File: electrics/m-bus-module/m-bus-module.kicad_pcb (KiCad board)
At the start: 2 copper layers, 86 x 31 mm, 58 parts, among them J1 North, J2 South, J3 West, J4 East, Q1 BC856B-13-F, Q2 BC846B-7-F, Q3 FDN5618P, U1 BA033CC0FP-E2, U2 MAX3486, U3 VOM452T, U4 VOM452T, U5 MC33072ADR2G, U6 LM4040DIM3-5.0/NOPB

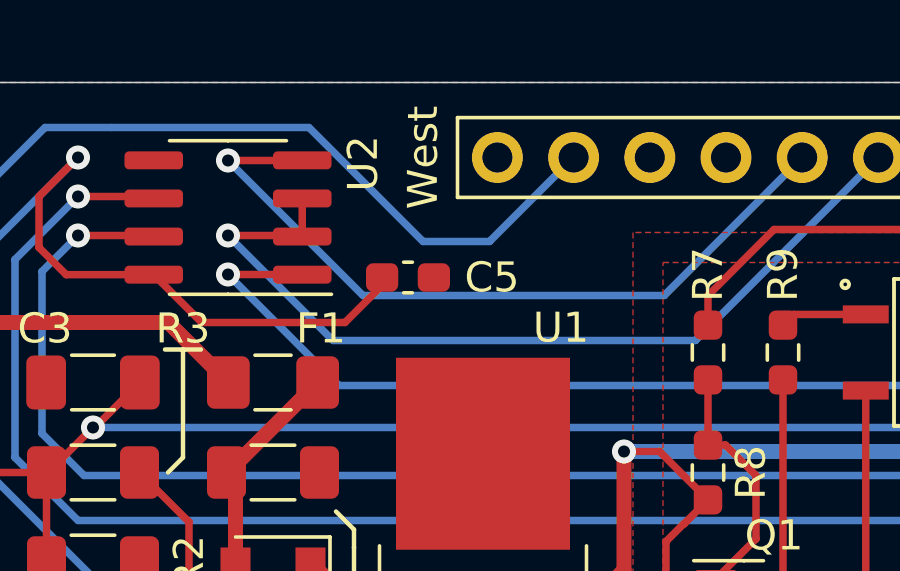
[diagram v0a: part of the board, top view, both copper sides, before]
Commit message: Fix all ERC and DRC warnings during build
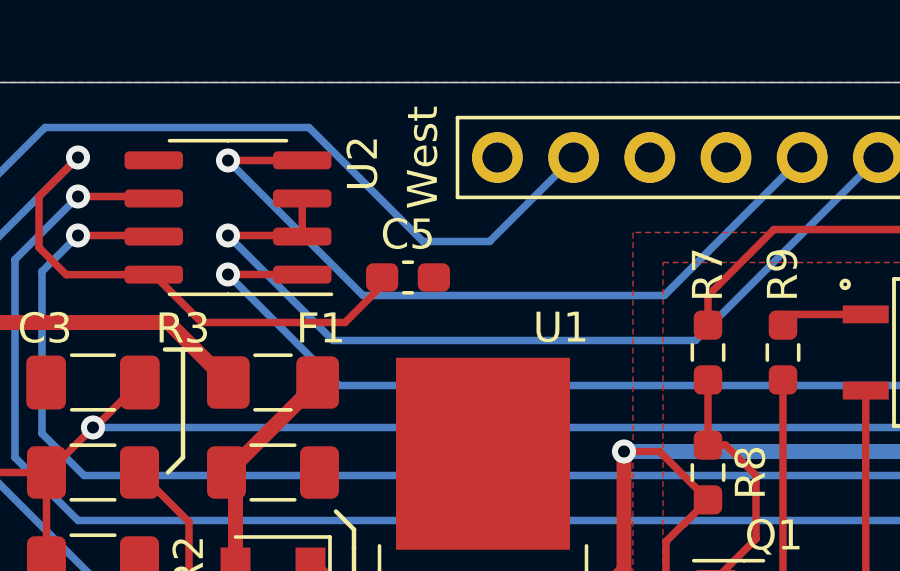
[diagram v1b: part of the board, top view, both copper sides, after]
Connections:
- net M-Bus-1 renamed M-Bus
- net M-Bus-2 renamed GNDS
- net VBUS+ renamed VBUS
